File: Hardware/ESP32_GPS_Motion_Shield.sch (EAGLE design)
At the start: 38 parts, among them J2 MICRO-SD_CARD_SOCKET, J6 3-PIN SMD, U1 LSM9DS1

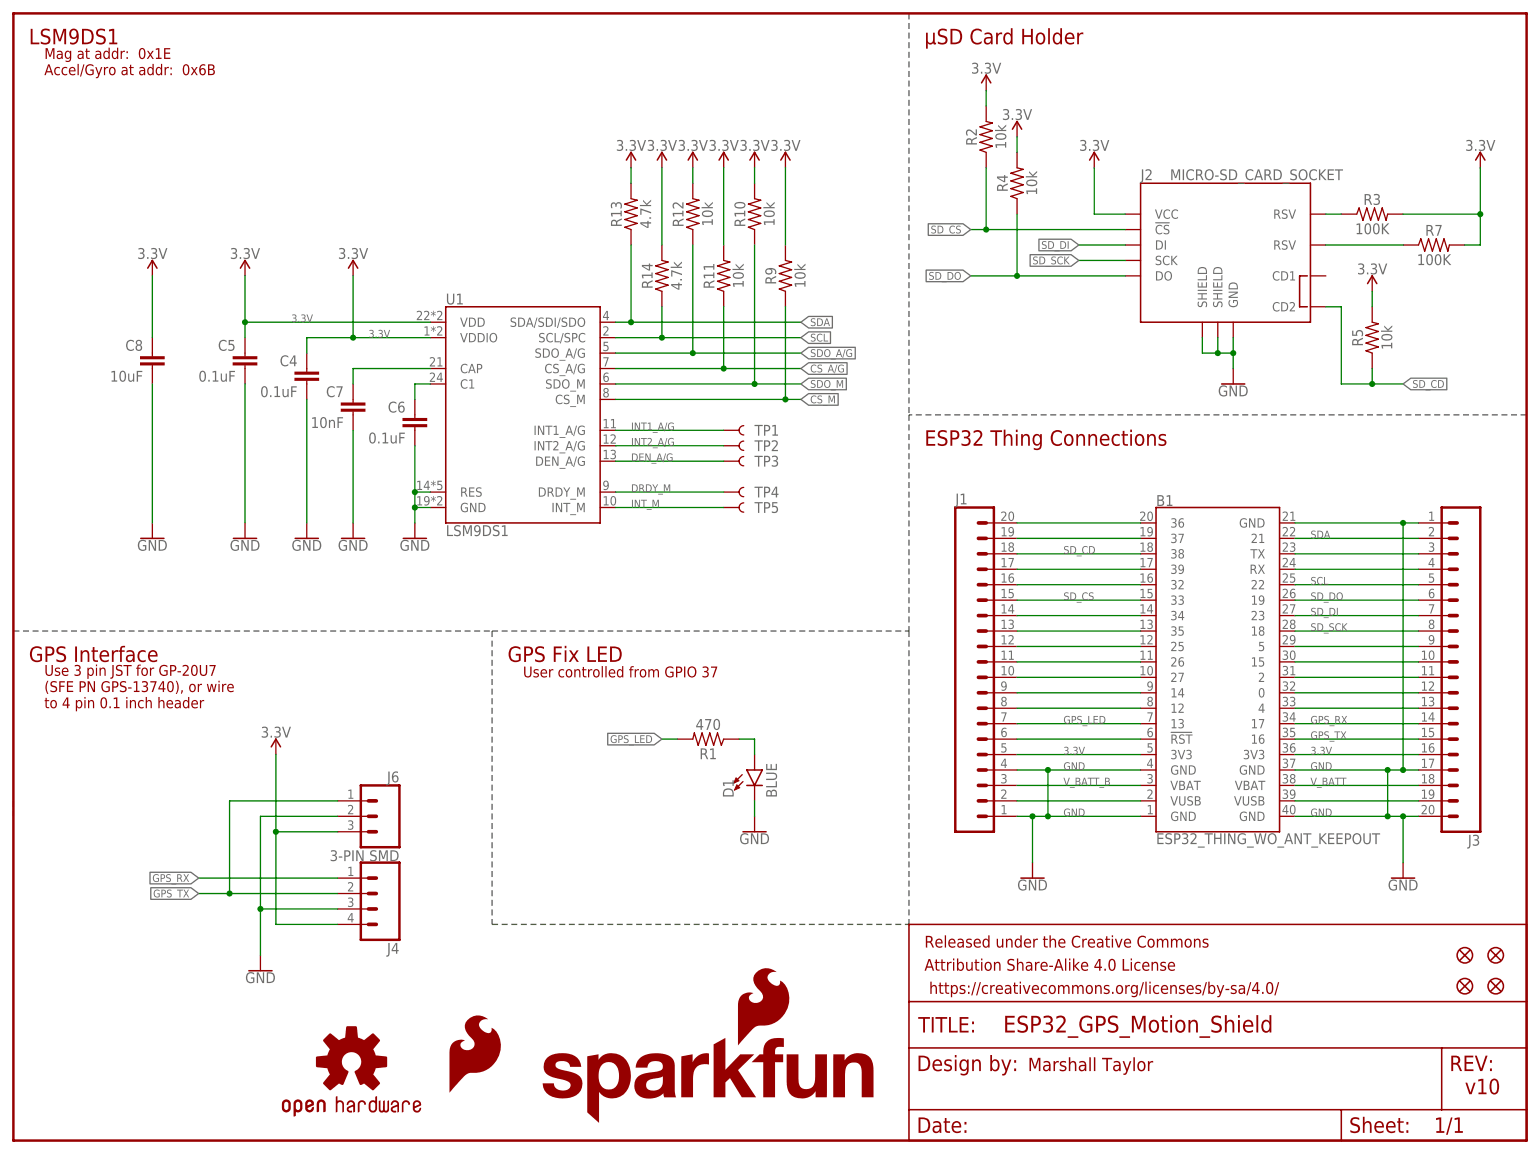
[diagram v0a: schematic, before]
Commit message: Double checked layout vs. fixed proto.  Adjusted small shapes.
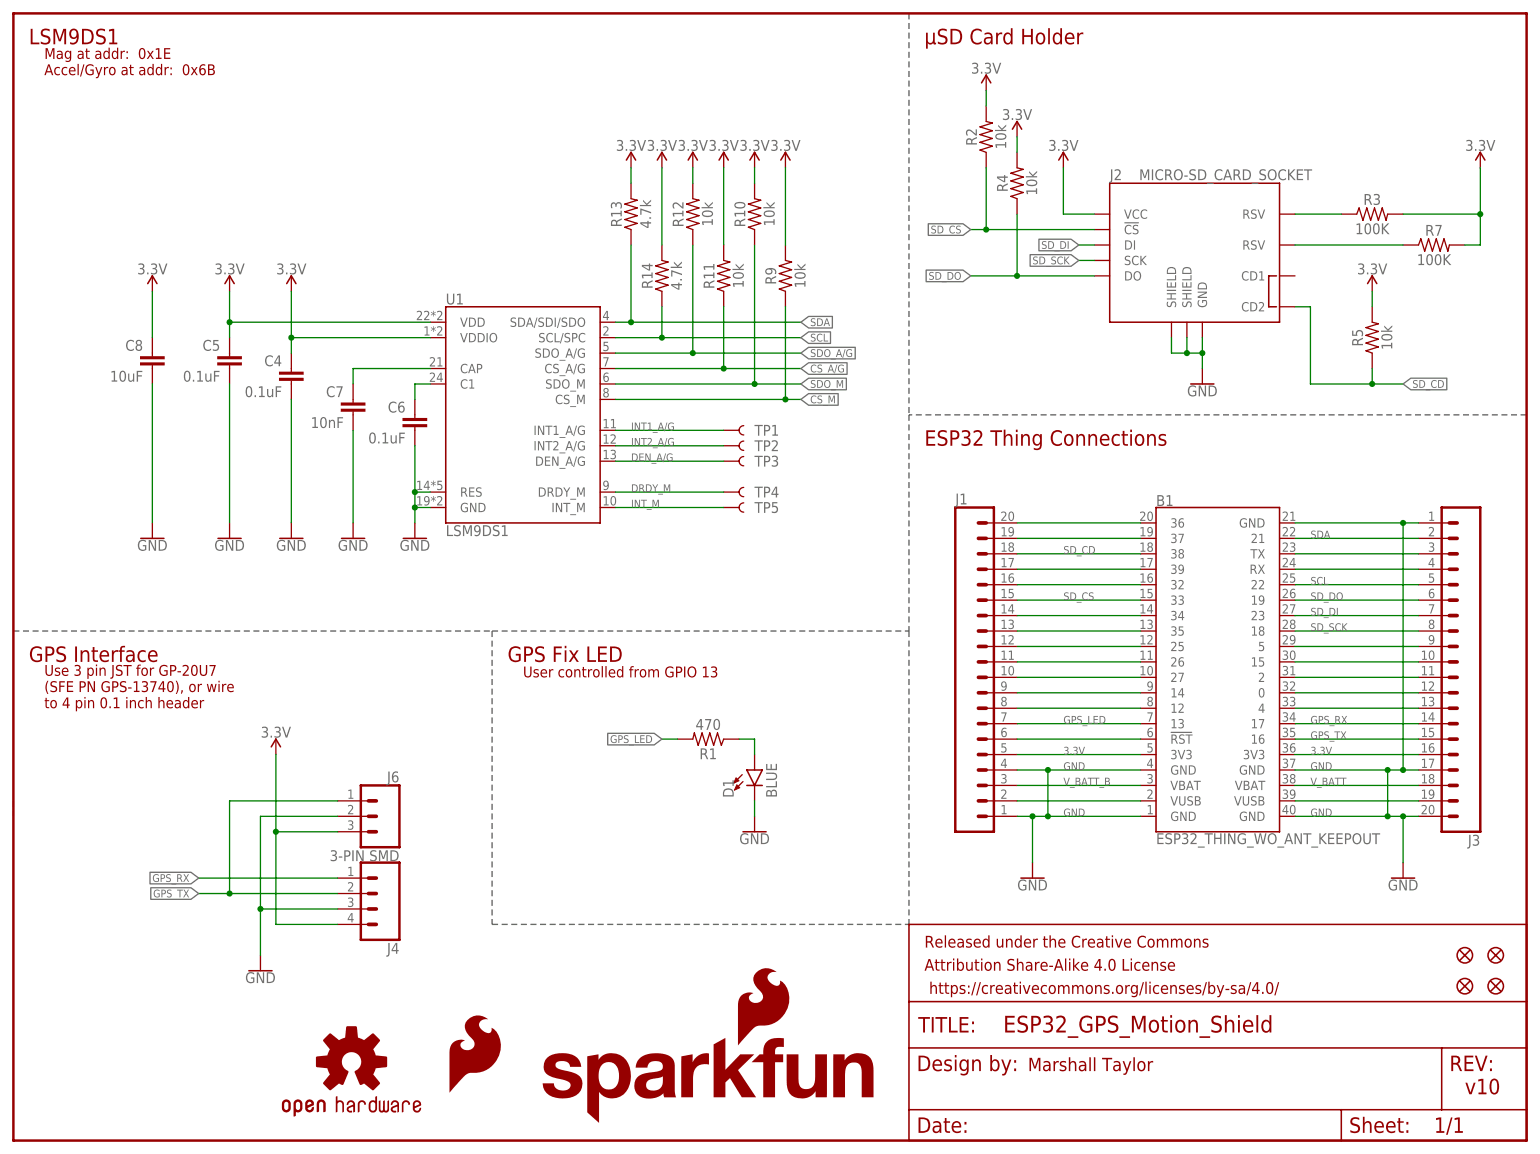
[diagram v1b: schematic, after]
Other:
- note added: "User controlled from GPIO 13"
- note removed: "User controlled from GPIO 37"
- moved on the sheet: C4, C5, J2

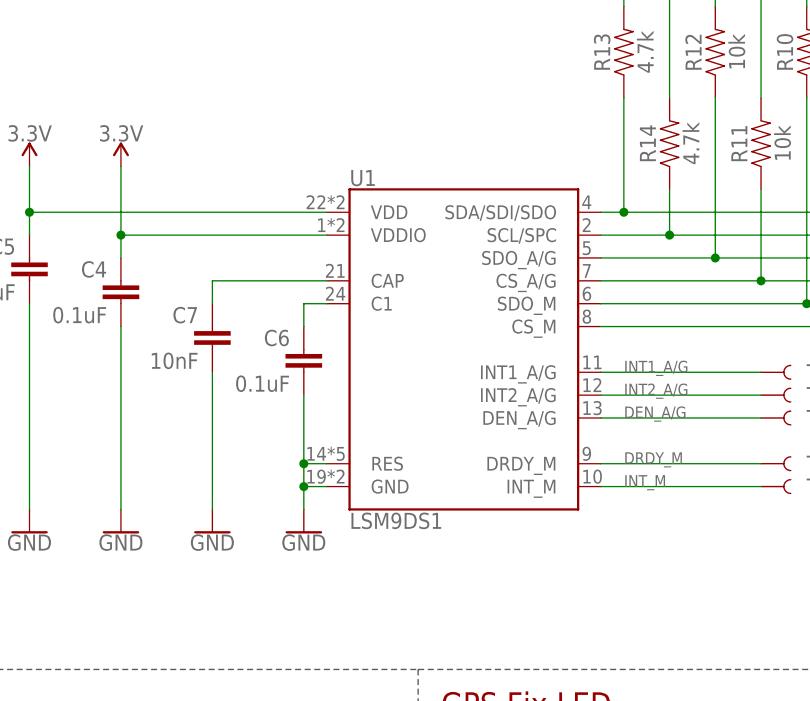
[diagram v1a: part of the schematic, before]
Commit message: Fixed items from redboard review
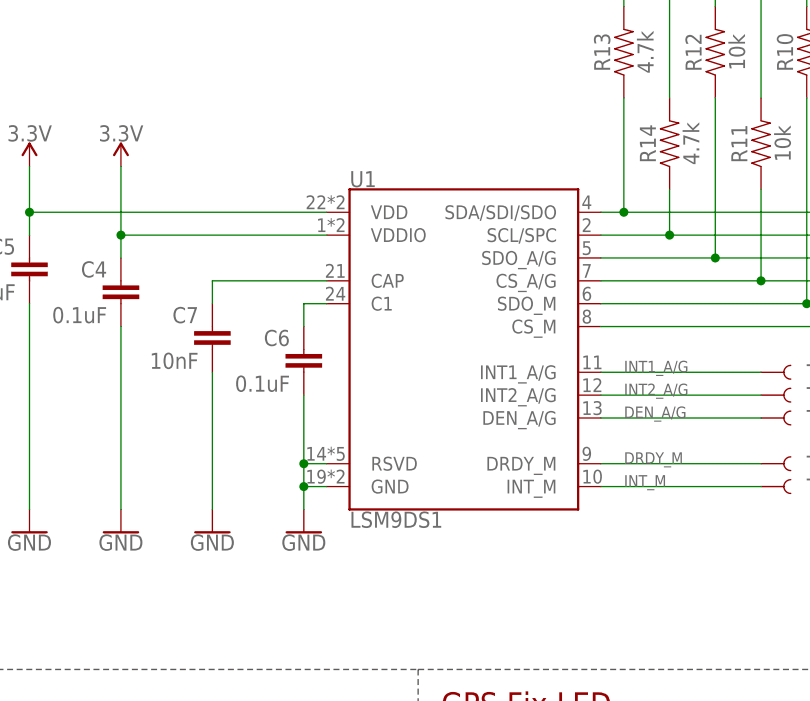
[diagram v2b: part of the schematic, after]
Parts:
- U1: device LSM9DS1_temp:LSM9DS1 -> SparkFun-Sensors:LSM9DS1
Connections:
- net GND: now also U1.RSVD; no longer U1.RES
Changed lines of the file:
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@@
 <part name="GND6" library="SparkFun-PowerSymbols" deviceset="GND" device=""/>
 <part name="GND7" library="SparkFun-PowerSymbols" deviceset="GND" device=""/>
-<part name="U1" library="LSM9DS1_temp" deviceset="LSM9DS1" device=""/>
+<part name="U1" library="SparkFun-Sensors" deviceset="LSM9DS1" device=""/>
 <part name="C4" library="SparkFun-Capacitors" deviceset="0.1UF" device="-0402-16V-10%" value="0.1uF"/>
 <part name="C5" library="SparkFun-Capacitors" deviceset="0.1UF" device="-0402-16V-10%" value="0.1uF"/>
@@
 </segment>
 <segment>
-<pinref part="U1" gate="G$1" pin="RES"/>
+<pinref part="U1" gate="G$1" pin="RSVD"/>
 <wire x1="68.58" y1="106.68" x2="66.04" y2="106.68" width="0.1524" layer="91"/>
 <wire x1="66.04" y1="106.68" x2="66.04" y2="104.14" width="0.1524" layer="91"/>
@@
 </sheet>
 </sheets>
+<errors>
+</errors>
 </schematic>
 </drawing>
